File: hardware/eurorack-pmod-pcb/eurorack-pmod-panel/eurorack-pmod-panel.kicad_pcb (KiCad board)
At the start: 2 copper layers, 30 x 128.5 mm, 11 parts

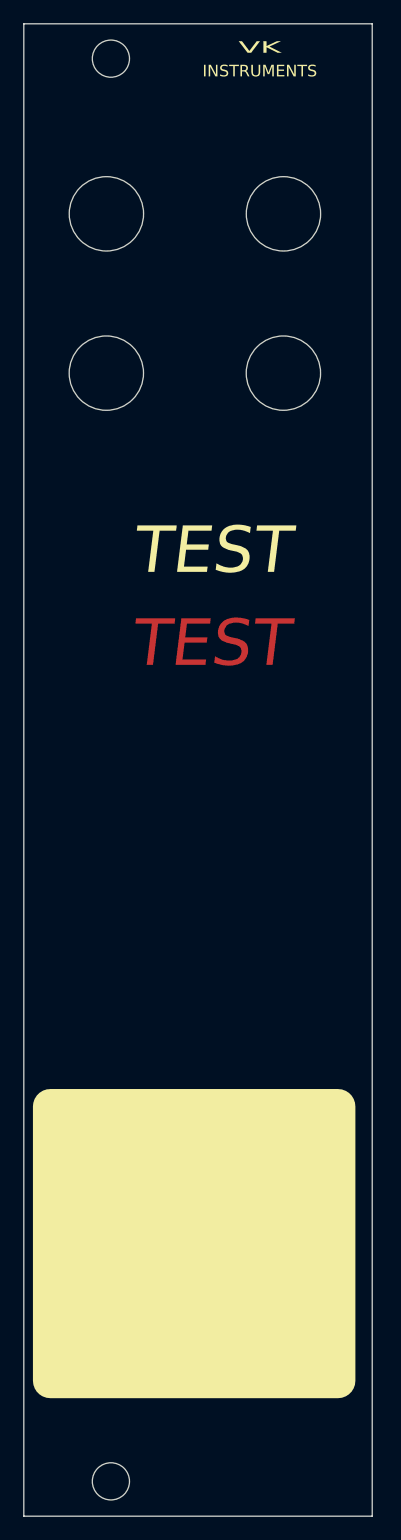
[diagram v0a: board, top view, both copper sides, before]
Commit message: Finish panel and send for fab1
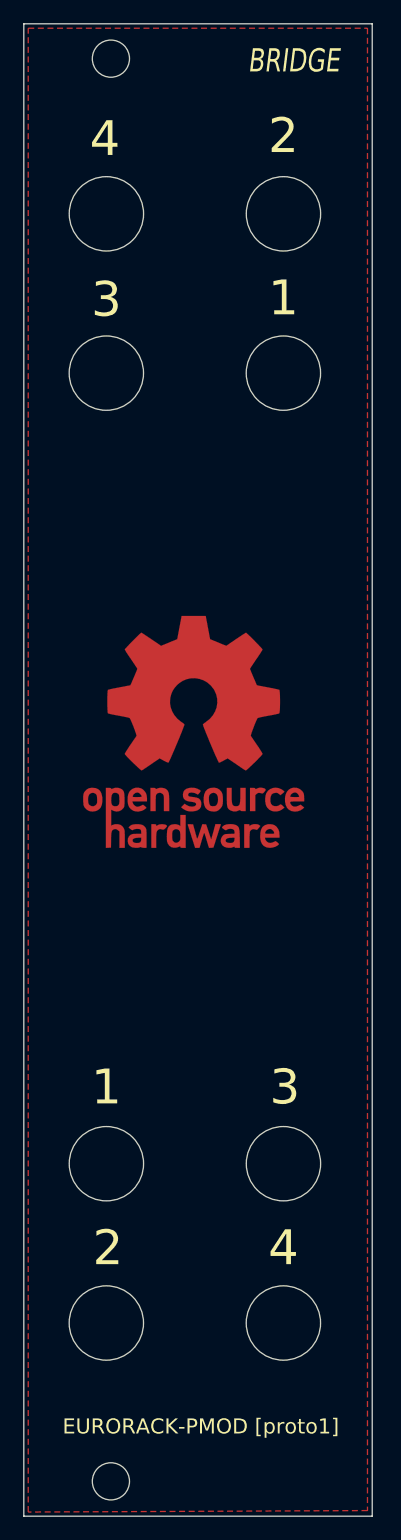
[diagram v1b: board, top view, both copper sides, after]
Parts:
- added REF**: OSHW-Logo_19x20mm_Copper, Symbol:OSHW-Logo_19x20mm_Copper, F.Cu at (14.6, 61.0)
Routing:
- added copper zone on F.Cu, net (none)
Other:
- board text added: "1"
- board text added: "2"
- board text added: "3"
- board text added: "4"
- board text added: "BRIDGE"
- board text added: "EURORACK-PMOD [proto1]"
- board text added: "IN"
- board text added: "OUT"
- board text added: "PMOD"
- board text added: "VK2SEB"
- board text removed: "INSTRUMENTS"
- board text removed: "TEST"
- board text removed: "VK"
